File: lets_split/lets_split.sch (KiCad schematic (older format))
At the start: 67 parts, among them J1 3PIN, J2 6PIN, J3 3PIN, J4 CON1, J5 CON1, J6 CON1, J7 CON1, J8 CON1, J9 CON1, SW1 SW_PUSH, SW10 SW_PUSH, SW11 SW_PUSH, SW12 SW_PUSH, SW13 SW_PUSH, SW14 SW_PUSH, SW15 SW_PUSH, SW16 SW_PUSH, SW17 SW_PUSH, SW18 SW_PUSH, SW19 SW_PUSH, SW2 SW_PUSH, SW20 SW_PUSH, SW21 SW_PUSH, SW22 SW_PUSH, SW23 SW_PUSH, SW24 SW_PUSH, SW3 SW_PUSH, SW4 SW_PUSH, SW5 SW_PUSH, SW6 SW_PUSH, SW7 SW_PUSH, SW8 SW_PUSH, SW9 SW_PUSH, U1 ProMicro, U2 HOLE, U3 HOLE, U4 HOLE, U5 HOLE

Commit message: Simplify jumper for pin selection of TSSR jack
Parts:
- J1, J3: footprint prettylib:jumper -> local:SMD_JUMPER_2
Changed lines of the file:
@@
 F 0 "J1" H 5750 2250 60  0000 C CNN
 F 1 "3PIN" H 5750 1850 60  0000 C CNN
-F 2 "prettylib:jumper" H 5800 2050 60  0001 C CNN
+F 2 "local:SMD_JUMPER_2" H 5800 2050 60  0001 C CNN
 F 3 "" H 5800 2050 60  0000 C CNN
 	1    5800 2050
@@
 F 0 "J3" H 7450 2250 60  0000 C CNN
 F 1 "3PIN" H 7450 1850 60  0000 C CNN
-F 2 "prettylib:jumper" H 7500 2050 60  0001 C CNN
+F 2 "local:SMD_JUMPER_2" H 7500 2050 60  0001 C CNN
 F 3 "" H 7500 2050 60  0000 C CNN
 	1    7500 2050

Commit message: Replace switch module without oval holes
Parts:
- SW1, SW10, SW11, SW12, SW13, SW14, SW15, SW16, SW17, SW18, SW19, SW2, SW20, SW21, SW22, SW23, SW24, SW3, SW4, SW5, SW6, SW7, SW8, SW9: footprint flipalps:MXALPS_FLIP -> local:MXALPS_FLIP_HOLES
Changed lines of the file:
@@
 F 0 "SW1" H 5600 3310 50  0000 C CNN
 F 1 "SW_PUSH" H 5450 3120 50  0000 C CNN
-F 2 "flipalps:MXALPS_FLIP" H 5450 3200 50  0001 C CNN
+F 2 "local:MXALPS_FLIP_HOLES" H 5450 3200 50  0001 C CNN
 F 3 "" H 5450 3200 50  0000 C CNN
 	1    5450 3200
@@
 F 0 "SW5" H 6350 3310 50  0000 C CNN
 F 1 "SW_PUSH" H 6200 3120 50  0000 C CNN
-F 2 "flipalps:MXALPS_FLIP" H 6200 3200 50  0001 C CNN
+F 2 "local:MXALPS_FLIP_HOLES" H 6200 3200 50  0001 C CNN
 F 3 "" H 6200 3200 50  0000 C CNN
 	1    6200 3200
@@
 F 0 "SW9" H 7050 3310 50  0000 C CNN
 F 1 "SW_PUSH" H 6900 3120 50  0000 C CNN
-F 2 "flipalps:MXALPS_FLIP" H 6900 3200 50  0001 C CNN
+F 2 "local:MXALPS_FLIP_HOLES" H 6900 3200 50  0001 C CNN
 F 3 "" H 6900 3200 50  0000 C CNN
 	1    6900 3200
@@
 F 0 "SW13" H 7800 3310 50  0000 C CNN
 F 1 "SW_PUSH" H 7650 3120 50  0000 C CNN
-F 2 "flipalps:MXALPS_FLIP" H 7650 3200 50  0001 C CNN
+F 2 "local:MXALPS_FLIP_HOLES" H 7650 3200 50  0001 C CNN
 F 3 "" H 7650 3200 50  0000 C CNN
 	1    7650 3200
@@
 F 0 "SW17" H 8550 3310 50  0000 C CNN
 F 1 "SW_PUSH" H 8400 3120 50  0000 C CNN
-F 2 "flipalps:MXALPS_FLIP" H 8400 3200 50  0001 C CNN
+F 2 "local:MXALPS_FLIP_HOLES" H 8400 3200 50  0001 C CNN
 F 3 "" H 8400 3200 50  0000 C CNN
 	1    8400 3200
@@
 F 0 "SW21" H 9300 3310 50  0000 C CNN
 F 1 "SW_PUSH" H 9150 3120 50  0000 C CNN
-F 2 "flipalps:MXALPS_FLIP" H 9150 3200 50  0001 C CNN
+F 2 "local:MXALPS_FLIP_HOLES" H 9150 3200 50  0001 C CNN
 F 3 "" H 9150 3200 50  0000 C CNN
 	1    9150 3200
@@
 F 0 "SW2" H 5600 3810 50  0000 C CNN
 F 1 "SW_PUSH" H 5450 3620 50  0000 C CNN
-F 2 "flipalps:MXALPS_FLIP" H 5450 3700 50  0001 C CNN
+F 2 "local:MXALPS_FLIP_HOLES" H 5450 3700 50  0001 C CNN
 F 3 "" H 5450 3700 50  0000 C CNN
 	1    5450 3700
@@
 F 0 "SW6" H 6350 3810 50  0000 C CNN
 F 1 "SW_PUSH" H 6200 3620 50  0000 C CNN
-F 2 "flipalps:MXALPS_FLIP" H 6200 3700 50  0001 C CNN
+F 2 "local:MXALPS_FLIP_HOLES" H 6200 3700 50  0001 C CNN
 F 3 "" H 6200 3700 50  0000 C CNN
 	1    6200 3700
@@
 F 0 "SW10" H 7050 3810 50  0000 C CNN
 F 1 "SW_PUSH" H 6900 3620 50  0000 C CNN
-F 2 "flipalps:MXALPS_FLIP" H 6900 3700 50  0001 C CNN
+F 2 "local:MXALPS_FLIP_HOLES" H 6900 3700 50  0001 C CNN
 F 3 "" H 6900 3700 50  0000 C CNN
 	1    6900 3700
@@
 F 0 "SW14" H 7800 3810 50  0000 C CNN
 F 1 "SW_PUSH" H 7650 3620 50  0000 C CNN
-F 2 "flipalps:MXALPS_FLIP" H 7650 3700 50  0001 C CNN
+F 2 "local:MXALPS_FLIP_HOLES" H 7650 3700 50  0001 C CNN
 F 3 "" H 7650 3700 50  0000 C CNN
 	1    7650 3700
@@
 F 0 "SW18" H 8550 3810 50  0000 C CNN
 F 1 "SW_PUSH" H 8400 3620 50  0000 C CNN
-F 2 "flipalps:MXALPS_FLIP" H 8400 3700 50  0001 C CNN
+F 2 "local:MXALPS_FLIP_HOLES" H 8400 3700 50  0001 C CNN
 F 3 "" H 8400 3700 50  0000 C CNN
 	1    8400 3700
@@
 F 0 "SW22" H 9300 3810 50  0000 C CNN
 F 1 "SW_PUSH" H 9150 3620 50  0000 C CNN
-F 2 "flipalps:MXALPS_FLIP" H 9150 3700 50  0001 C CNN
+F 2 "local:MXALPS_FLIP_HOLES" H 9150 3700 50  0001 C CNN
 F 3 "" H 9150 3700 50  0000 C CNN
 	1    9150 3700
@@
 F 0 "SW3" H 5600 4310 50  0000 C CNN
 F 1 "SW_PUSH" H 5450 4120 50  0000 C CNN
-F 2 "flipalps:MXALPS_FLIP" H 5450 4200 50  0001 C CNN
+F 2 "local:MXALPS_FLIP_HOLES" H 5450 4200 50  0001 C CNN
 F 3 "" H 5450 4200 50  0000 C CNN
 	1    5450 4200
@@
 F 0 "SW7" H 6350 4310 50  0000 C CNN
 F 1 "SW_PUSH" H 6200 4120 50  0000 C CNN
-F 2 "flipalps:MXALPS_FLIP" H 6200 4200 50  0001 C CNN
+F 2 "local:MXALPS_FLIP_HOLES" H 6200 4200 50  0001 C CNN
 F 3 "" H 6200 4200 50  0000 C CNN
 	1    6200 4200
@@
 F 0 "SW11" H 7050 4310 50  0000 C CNN
 F 1 "SW_PUSH" H 6900 4120 50  0000 C CNN
-F 2 "flipalps:MXALPS_FLIP" H 6900 4200 50  0001 C CNN
+F 2 "local:MXALPS_FLIP_HOLES" H 6900 4200 50  0001 C CNN
 F 3 "" H 6900 4200 50  0000 C CNN
 	1    6900 4200
@@
 F 0 "SW15" H 7800 4310 50  0000 C CNN
 F 1 "SW_PUSH" H 7650 4120 50  0000 C CNN
-F 2 "flipalps:MXALPS_FLIP" H 7650 4200 50  0001 C CNN
+F 2 "local:MXALPS_FLIP_HOLES" H 7650 4200 50  0001 C CNN
 F 3 "" H 7650 4200 50  0000 C CNN
 	1    7650 4200
@@
 F 0 "SW19" H 8550 4310 50  0000 C CNN
 F 1 "SW_PUSH" H 8400 4120 50  0000 C CNN
-F 2 "flipalps:MXALPS_FLIP" H 8400 4200 50  0001 C CNN
+F 2 "local:MXALPS_FLIP_HOLES" H 8400 4200 50  0001 C CNN
 F 3 "" H 8400 4200 50  0000 C CNN
 	1    8400 4200
@@
 F 0 "SW23" H 9300 4310 50  0000 C CNN
 F 1 "SW_PUSH" H 9150 4120 50  0000 C CNN
-F 2 "flipalps:MXALPS_FLIP" H 9150 4200 50  0001 C CNN
+F 2 "local:MXALPS_FLIP_HOLES" H 9150 4200 50  0001 C CNN
 F 3 "" H 9150 4200 50  0000 C CNN
 	1    9150 4200
@@
 F 0 "SW4" H 5600 4810 50  0000 C CNN
 F 1 "SW_PUSH" H 5450 4620 50  0000 C CNN
-F 2 "flipalps:MXALPS_FLIP" H 5450 4700 50  0001 C CNN
+F 2 "local:MXALPS_FLIP_HOLES" H 5450 4700 50  0001 C CNN
 F 3 "" H 5450 4700 50  0000 C CNN
 	1    5450 4700
@@
 F 0 "SW8" H 6350 4810 50  0000 C CNN
 F 1 "SW_PUSH" H 6200 4620 50  0000 C CNN
-F 2 "flipalps:MXALPS_FLIP" H 6200 4700 50  0001 C CNN
+F 2 "local:MXALPS_FLIP_HOLES" H 6200 4700 50  0001 C CNN
 F 3 "" H 6200 4700 50  0000 C CNN
 	1    6200 4700
@@
 F 0 "SW12" H 7050 4810 50  0000 C CNN
 F 1 "SW_PUSH" H 6900 4620 50  0000 C CNN
-F 2 "flipalps:MXALPS_FLIP" H 6900 4700 50  0001 C CNN
+F 2 "local:MXALPS_FLIP_HOLES" H 6900 4700 50  0001 C CNN
 F 3 "" H 6900 4700 50  0000 C CNN
 	1    6900 4700
@@
 F 0 "SW16" H 7800 4810 50  0000 C CNN
 F 1 "SW_PUSH" H 7650 4620 50  0000 C CNN
-F 2 "flipalps:MXALPS_FLIP" H 7650 4700 50  0001 C CNN
+F 2 "local:MXALPS_FLIP_HOLES" H 7650 4700 50  0001 C CNN
 F 3 "" H 7650 4700 50  0000 C CNN
 	1    7650 4700
@@
 F 0 "SW20" H 8550 4810 50  0000 C CNN
 F 1 "SW_PUSH" H 8400 4620 50  0000 C CNN
-F 2 "flipalps:MXALPS_FLIP" H 8400 4700 50  0001 C CNN
+F 2 "local:MXALPS_FLIP_HOLES" H 8400 4700 50  0001 C CNN
 F 3 "" H 8400 4700 50  0000 C CNN
 	1    8400 4700
@@
 F 0 "SW24" H 9300 4810 50  0000 C CNN
 F 1 "SW_PUSH" H 9150 4620 50  0000 C CNN
-F 2 "flipalps:MXALPS_FLIP" H 9150 4700 50  0001 C CNN
+F 2 "local:MXALPS_FLIP_HOLES" H 9150 4700 50  0001 C CNN
 F 3 "" H 9150 4700 50  0000 C CNN
 	1    9150 4700

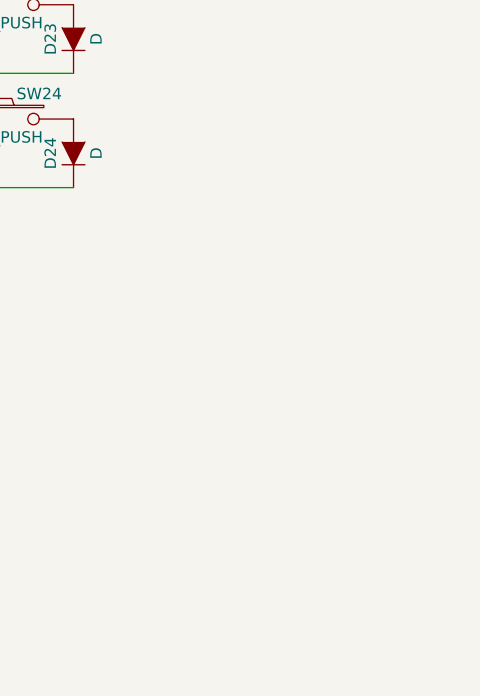
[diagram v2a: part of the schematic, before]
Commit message: Add fiducial marks
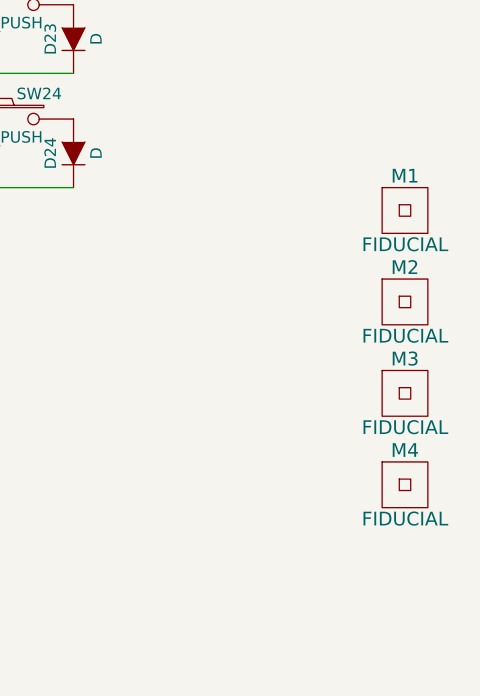
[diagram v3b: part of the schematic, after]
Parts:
- added M1, M2, M3, M4: FIDUCIAL, local:Fiducial_Mark, symbol FIDUCIAL
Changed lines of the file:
@@
 Text GLabel 1250 4000 2    60   Input ~ 0
 xtradata
+$Comp
+L FIDUCIAL M1
+U 1 1 59A57C29
+P 10900 5100
+F 0 "M1" H 10900 5250 60  0000 C CNN
+F 1 "FIDUCIAL" H 10900 4950 60  0000 C CNN
+F 2 "local:Fiducial_Mark" H 10900 5100 60  0001 C CNN
+F 3 "" H 10900 5100 60  0001 C CNN
+	1    10900 5100
+	1    0    0    -1
+$EndComp
+$Comp
+L FIDUCIAL M2
+U 1 1 59A58677
+P 10900 5500
+F 0 "M2" H 10900 5650 60  0000 C CNN
+F 1 "FIDUCIAL" H 10900 5350 60  0000 C CNN
+F 2 "local:Fiducial_Mark" H 10900 5500 60  0001 C CNN
+F 3 "" H 10900 5500 60  0001 C CNN
+	1    10900 5500
+	1    0    0    -1
+$EndComp
+$Comp
+L FIDUCIAL M3
+U 1 1 59A58764
+P 10900 5900
+F 0 "M3" H 10900 6050 60  0000 C CNN
+F 1 "FIDUCIAL" H 10900 5750 60  0000 C CNN
+F 2 "local:Fiducial_Mark" H 10900 5900 60  0001 C CNN
+F 3 "" H 10900 5900 60  0001 C CNN
+	1    10900 5900
+	1    0    0    -1
+$EndComp
+$Comp
+L FIDUCIAL M4
+U 1 1 59A58854
+P 10900 6300
+F 0 "M4" H 10900 6450 60  0000 C CNN
+F 1 "FIDUCIAL" H 10900 6150 60  0000 C CNN
+F 2 "local:Fiducial_Mark" H 10900 6300 60  0001 C CNN
+F 3 "" H 10900 6300 60  0001 C CNN
+	1    10900 6300
+	1    0    0    -1
+$EndComp
 $EndSCHEMATC

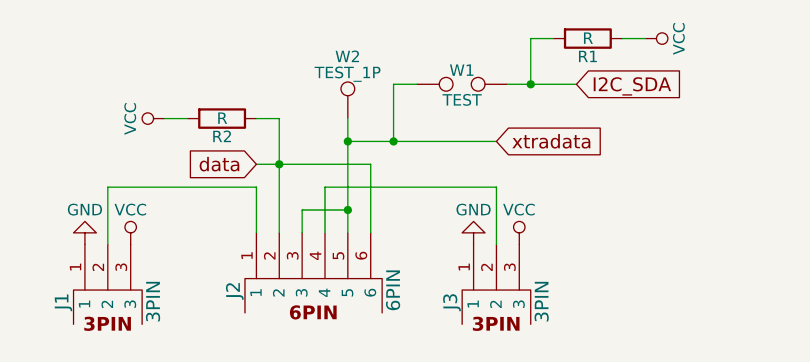
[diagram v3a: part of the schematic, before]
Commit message: Add resistor value for I2C
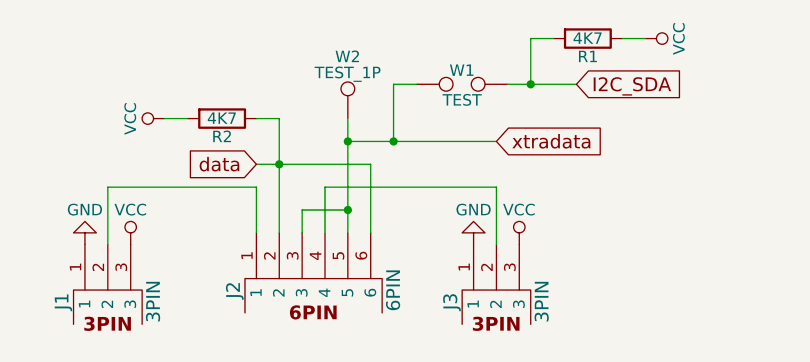
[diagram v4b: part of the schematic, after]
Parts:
- R1, R2: value R -> 4K7
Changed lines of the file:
@@
 P 6300 1300
 F 0 "R2" V 6380 1300 50  0000 C CNN
-F 1 "R" V 6300 1300 50  0000 C CNN
+F 1 "4K7" V 6300 1300 50  0000 C CNN
 F 2 "local:RESISTOR" V 6230 1300 50  0001 C CNN
 F 3 "" H 6300 1300 50  0000 C CNN
@@
 P 7900 950
 F 0 "R1" V 7980 950 50  0000 C CNN
-F 1 "R" V 7900 950 50  0000 C CNN
+F 1 "4K7" V 7900 950 50  0000 C CNN
 F 2 "local:RESISTOR" V 7830 950 50  0001 C CNN
 F 3 "" H 7900 950 50  0000 C CNN

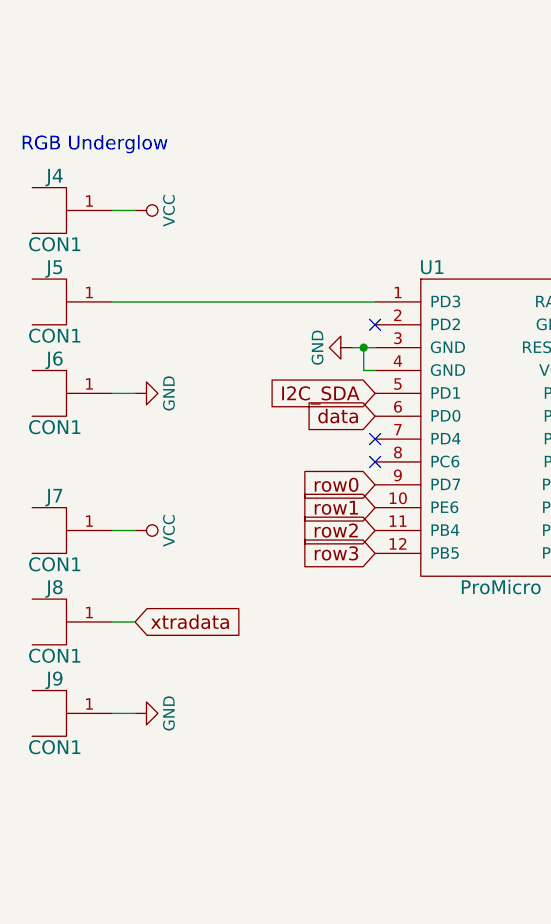
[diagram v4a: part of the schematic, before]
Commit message: Put pads for RGB strip into single module
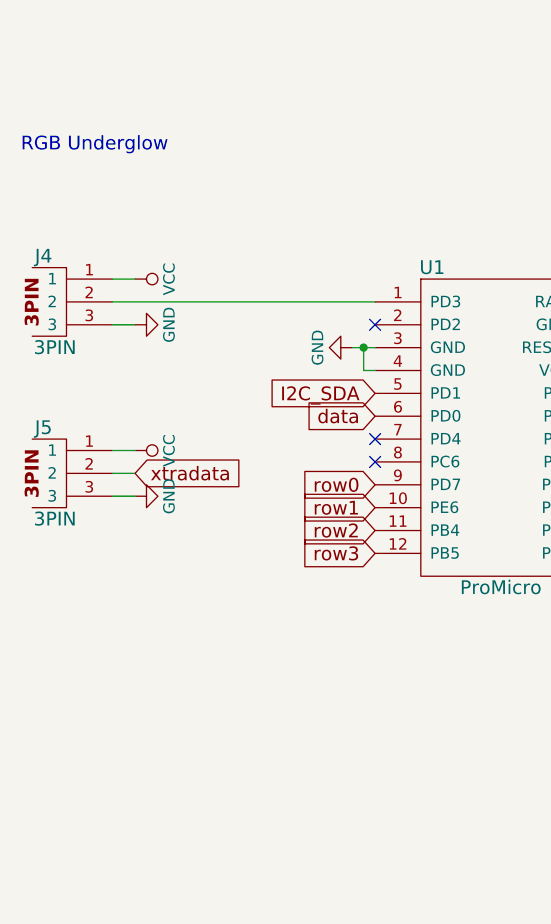
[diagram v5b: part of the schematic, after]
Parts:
- removed J4, J5, J6, J7, J8, J9: CON1, local:CON1_SMD_BOTH, symbol 1PIN
- added J4, J5: 3PIN, local:CON3_SMD_BOTH, symbol 3PIN
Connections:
- net GND: now also J4.3, J5.3
- net VCC: now also J4.1, J5.1
- net xtradata: now also J5.2
- net at U1.1 (PD3): now also J4.2
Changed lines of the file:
@@
 NoConn ~ 3400 3000
 NoConn ~ 3400 3100
-$Comp
-L 1PIN J5
-U 1 1 59A446B6
-P 900 2600
-F 0 "J5" H 900 2750 60  0000 C CNN
-F 1 "CON1" H 900 2450 60  0000 C CNN
-F 2 "local:CON1_SMD_BOTH" H 850 2600 60  0001 C CNN
-F 3 "" H 850 2600 60  0001 C CNN
-	1    900  2600
-	1    0    0    -1
-$EndComp
 Wire Wire Line
 	1150 2600 2300 2600
@@
 L VCC #PWR011
 U 1 1 59A522C2
-P 1250 2200
-F 0 "#PWR011" H 1250 2050 50  0001 C CNN
-F 1 "VCC" H 1250 2350 50  0000 C CNN
-F 2 "" H 1250 2200 50  0000 C CNN
-F 3 "" H 1250 2200 50  0000 C CNN
-	1    1250 2200
+P 1250 2500
+F 0 "#PWR011" H 1250 2350 50  0001 C CNN
+F 1 "VCC" H 1250 2650 50  0000 C CNN
+F 2 "" H 1250 2500 50  0000 C CNN
+F 3 "" H 1250 2500 50  0000 C CNN
+	1    1250 2500
 	0    1    1    0
 $EndComp
@@
 L GND #PWR012
 U 1 1 59A523C9
-P 1250 3000
-F 0 "#PWR012" H 1250 2750 50  0001 C CNN
-F 1 "GND" H 1250 2850 50  0000 C CNN
-F 2 "" H 1250 3000 50  0000 C CNN
-F 3 "" H 1250 3000 50  0000 C CNN
-	1    1250 3000
+P 1250 2700
+F 0 "#PWR012" H 1250 2450 50  0001 C CNN
+F 1 "GND" H 1250 2550 50  0000 C CNN
+F 2 "" H 1250 2700 50  0000 C CNN
+F 3 "" H 1250 2700 50  0000 C CNN
+	1    1250 2700
 	0    -1   -1   0
 $EndComp
 Wire Wire Line
-	1250 3000 1150 3000
-$Comp
-L 1PIN J4
-U 1 1 59A54755
-P 900 2200
-F 0 "J4" H 900 2350 60  0000 C CNN
-F 1 "CON1" H 900 2050 60  0000 C CNN
-F 2 "local:CON1_SMD_BOTH" H 850 2200 60  0001 C CNN
-F 3 "" H 850 2200 60  0001 C CNN
-	1    900  2200
-	1    0    0    -1
-$EndComp
-$Comp
-L 1PIN J6
-U 1 1 59A547F9
-P 900 3000
-F 0 "J6" H 900 3150 60  0000 C CNN
-F 1 "CON1" H 900 2850 60  0000 C CNN
-F 2 "local:CON1_SMD_BOTH" H 850 3000 60  0001 C CNN
-F 3 "" H 850 3000 60  0001 C CNN
-	1    900  3000
-	1    0    0    -1
-$EndComp
-Wire Wire Line
-	1250 2200 1150 2200
+	1250 2700 1150 2700
+Wire Wire Line
+	1250 2500 1150 2500
 $Comp
 L VCC #PWR013
 U 1 1 59A52B8D
-P 1250 3600
-F 0 "#PWR013" H 1250 3450 50  0001 C CNN
-F 1 "VCC" H 1250 3750 50  0000 C CNN
-F 2 "" H 1250 3600 50  0000 C CNN
-F 3 "" H 1250 3600 50  0000 C CNN
-	1    1250 3600
+P 1250 3250
+F 0 "#PWR013" H 1250 3100 50  0001 C CNN
+F 1 "VCC" H 1250 3400 50  0000 C CNN
+F 2 "" H 1250 3250 50  0000 C CNN
+F 3 "" H 1250 3250 50  0000 C CNN
+	1    1250 3250
 	0    1    1    0
 $EndComp
@@
 L GND #PWR014
 U 1 1 59A52B93
-P 1250 4400
-F 0 "#PWR014" H 1250 4150 50  0001 C CNN
-F 1 "GND" H 1250 4250 50  0000 C CNN
-F 2 "" H 1250 4400 50  0000 C CNN
-F 3 "" H 1250 4400 50  0000 C CNN
-	1    1250 4400
+P 1250 3450
+F 0 "#PWR014" H 1250 3200 50  0001 C CNN
+F 1 "GND" H 1250 3300 50  0000 C CNN
+F 2 "" H 1250 3450 50  0000 C CNN
+F 3 "" H 1250 3450 50  0000 C CNN
+	1    1250 3450
 	0    -1   -1   0
 $EndComp
 Wire Wire Line
-	1250 4400 1150 4400
-$Comp
-L 1PIN J8
-U 1 1 59A52B9A
-P 900 4000
-F 0 "J8" H 900 4150 60  0000 C CNN
-F 1 "CON1" H 900 3850 60  0000 C CNN
-F 2 "local:CON1_SMD_BOTH" H 850 4000 60  0001 C CNN
-F 3 "" H 850 4000 60  0001 C CNN
-	1    900  4000
-	1    0    0    -1
-$EndComp
-$Comp
-L 1PIN J9
-U 1 1 59A52BA0
-P 900 4400
-F 0 "J9" H 900 4550 60  0000 C CNN
-F 1 "CON1" H 900 4250 60  0000 C CNN
-F 2 "local:CON1_SMD_BOTH" H 850 4400 60  0001 C CNN
-F 3 "" H 850 4400 60  0001 C CNN
-	1    900  4400
-	1    0    0    -1
-$EndComp
-Wire Wire Line
-	1250 3600 1150 3600
-$Comp
-L 1PIN J7
-U 1 1 59A52C6D
-P 900 3600
-F 0 "J7" H 900 3750 60  0000 C CNN
-F 1 "CON1" H 900 3450 60  0000 C CNN
-F 2 "local:CON1_SMD_BOTH" H 850 3600 60  0001 C CNN
-F 3 "" H 850 3600 60  0001 C CNN
-	1    900  3600
-	1    0    0    -1
-$EndComp
-Wire Wire Line
-	1150 4000 1250 4000
-Text GLabel 1250 4000 2    60   Input ~ 0
+	1250 3450 1150 3450
+Wire Wire Line
+	1250 3250 1150 3250
+Wire Wire Line
+	1150 3350 1250 3350
+Text GLabel 1250 3350 2    60   Input ~ 0
 xtradata
 $Comp
@@
 	1    0    0    -1
 $EndComp
+$Comp
+L 3PIN J5
+U 1 1 59A6A7A3
+P 950 3350
+F 0 "J5" H 850 3550 60  0000 C CNN
+F 1 "3PIN" H 900 3150 60  0000 C CNN
+F 2 "local:CON3_SMD_BOTH" H 950 3350 60  0001 C CNN
+F 3 "" H 950 3350 60  0000 C CNN
+	1    950  3350
+	1    0    0    -1
+$EndComp
+$Comp
+L 3PIN J4
+U 1 1 59A6BB29
+P 950 2600
+F 0 "J4" H 850 2800 60  0000 C CNN
+F 1 "3PIN" H 900 2400 60  0000 C CNN
+F 2 "local:CON3_SMD_BOTH" H 950 2600 60  0001 C CNN
+F 3 "" H 950 2600 60  0000 C CNN
+	1    950  2600
+	1    0    0    -1
+$EndComp

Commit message: Replace module for reset switch with one compatible to vertical type
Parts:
- RSW1: footprint local:SKHL -> local:TACTILE_COMPATIBLE
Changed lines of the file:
@@
 F 0 "RSW1" H 4150 2910 50  0000 C CNN
 F 1 "SW_PUSH" H 4000 2720 50  0000 C CNN
-F 2 "local:SKHL" H 4000 2800 50  0001 C CNN
+F 2 "local:TACTILE_COMPATIBLE" H 4000 2800 50  0001 C CNN
 F 3 "" H 4000 2800 50  0000 C CNN
 	1    4000 2800
